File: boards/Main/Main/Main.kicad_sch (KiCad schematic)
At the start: 28 parts, among them J1 CAN_H, J10 Status_Light, J11 J00-0045NL, J12 IMU, J2 GND, J3 TX/RX, J4 5V, J5 Digital I/O, J6 CAN_Board, J7 CAN_L, J8 CAN H/L, J9 24V, K1 G5LE-1, K3 G5LE-1, K4 G5LE-1, Q1 2N3904, Q2 2N3904, Q3 2N3904, U1 Teensy4.1

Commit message: Updated Main PCB
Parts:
- removed J8: CAN H/L, Connector_PinHeader_2.54mm:PinHeader_1x01_P2.54mm_Vertical, symbol Connector_Generic:Conn_02x09_Row_Letter_First
- added CAN_OUT1: CAN_pins, Connector_PinHeader_2.54mm:PinHeader_2x09_P2.54mm_Vertical, symbol Connector_Generic:Conn_02x09_Top_Bottom
- added Ethernet_Cable1: Conn_02x03_Odd_Even, Connector_PinHeader_2.54mm:PinHeader_2x03_P2.54mm_Vertical, symbol Connector_Generic:Conn_02x03_Odd_Even
- 5V_Pin1: renamed from J4; footprint Connector_PinHeader_2.54mm:PinHeader_1x04_P2.54mm_Vertical -> Connector_PinHeader_2.54mm:PinHeader_1x02_P2.54mm_Vertical
- C1: renamed from 0.1uF1; value C -> 0.1uF
- D1, D2, D3: footprint LED_THT:LED_D5.0mm-3 -> LED_THT:LED_D5.0mm
- Relay_1: renamed from K1; value G5LE-1 -> G5LE1_Green
- Relay_2: renamed from K4; value G5LE-1 -> G5LE1_Blue
- Relay_3: renamed from K3; value G5LE-1 -> G5LE1_Red
- renumbered J9 to 24V_Pin1, J6 to CAN_Board1, J1 to CAN_H1, J7 to CAN_L1, J5 to Digital_I/O1, J11 to Ethernet1, J2 to GND_Pin1, J12 to IMU1, Q2 to Q1, Q1 to Q2, J3 to RTX_Pin1, J10 to Status_Light1, U1 to Teensy4.1
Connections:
- net M1H: now also CAN_OUT1.10 (Pin_10), CAN_OUT1.12 (Pin_12), CAN_OUT1.14 (Pin_14), CAN_OUT1.16 (Pin_16), CAN_OUT1.18 (Pin_18), CAN_OUT1.2 (Pin_2), CAN_OUT1.4 (Pin_4), CAN_OUT1.6 (Pin_6), CAN_OUT1.8 (Pin_8)
- net M1L: now also CAN_OUT1.1 (Pin_1), CAN_OUT1.11 (Pin_11), CAN_OUT1.13 (Pin_13), CAN_OUT1.15 (Pin_15), CAN_OUT1.17 (Pin_17), CAN_OUT1.3 (Pin_3), CAN_OUT1.5 (Pin_5), CAN_OUT1.7 (Pin_7), CAN_OUT1.9 (Pin_9)
- net at Teensy4.1.60 (R+): no longer Ethernet1.3 (RD+)
- net at Teensy4.1.61 (LED): no longer Ethernet1.9 (LA)
- net at Teensy4.1.62 (T-): no longer Ethernet1.2 (TD-)
- net at Teensy4.1.63 (T+): no longer Ethernet1.1 (TD+)
- net at C1.2, Ethernet1.10 (LC), Ethernet1.8 (GND): now also Ethernet_Cable1.3 (Pin_3); no longer Teensy4.1.64 (GND)
- net at Teensy4.1.65 (R-): no longer Ethernet1.6 (RD-)
- new net: Ethernet1.1 (TD+), Ethernet_Cable1.5 (Pin_5)
- new net: Ethernet1.2 (TD-), Ethernet_Cable1.6 (Pin_6)
- new net: Ethernet1.3 (RD+), Ethernet_Cable1.2 (Pin_2)
- new net: Ethernet1.6 (RD-), Ethernet_Cable1.1 (Pin_1)
- new net: Ethernet1.9 (LA), Ethernet_Cable1.4 (Pin_4)
- no-connect marks 50 -> 56
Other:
- moved on the sheet: RTX_Pin1, Status_Light1

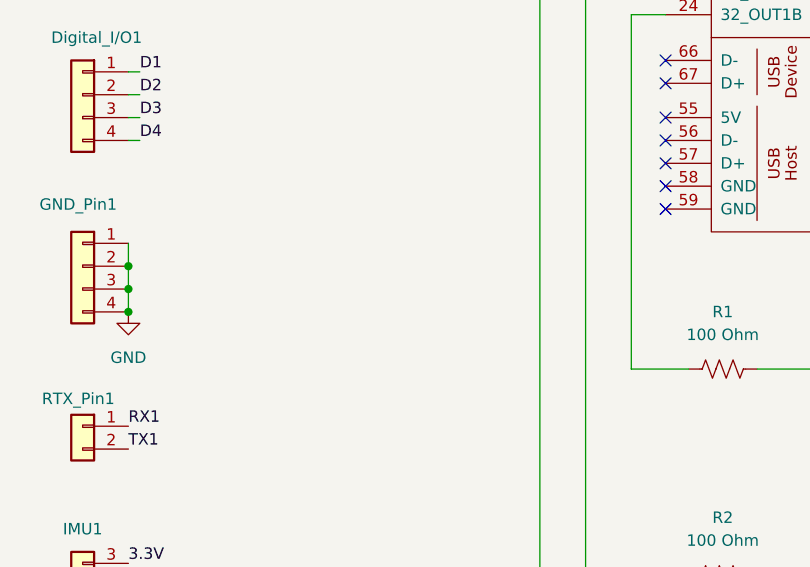
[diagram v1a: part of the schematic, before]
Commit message: Added Holes to Main PCB
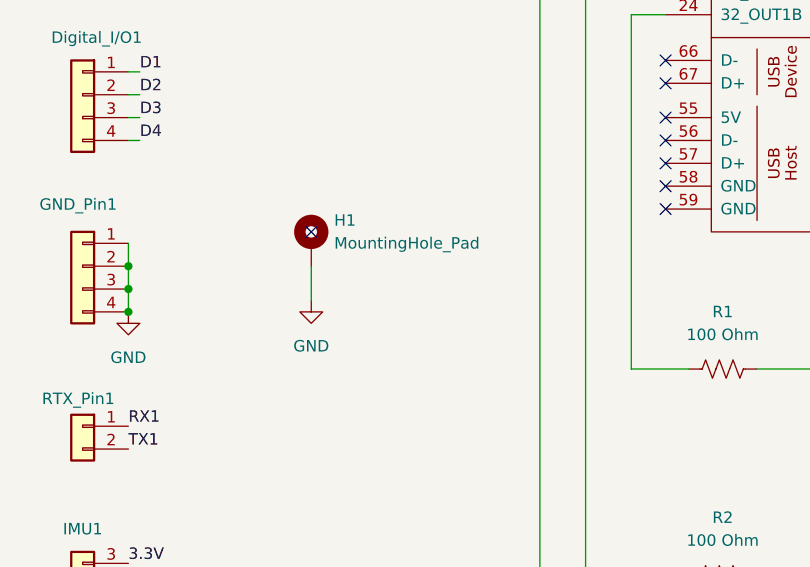
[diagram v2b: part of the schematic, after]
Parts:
- added H1: MountingHole_Pad, MountingHole:MountingHole_3.2mm_M3_DIN965_Pad_TopBottom, symbol Mechanical:MountingHole_Pad
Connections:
- net GND: now also H1.1
- no-connect marks 56 -> 57
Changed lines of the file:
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@@
+	)
+	(no_connect
+		(at 45.72 111.76)
 	)
 	(no_connect
@@
 		(pts
 			(xy 165.1 138.43) (xy 165.1 144.78)
+		)
+		(stroke
+			(width 0)
+			(type default)
+		)
+	)
+	(wire
+		(pts
+			(xy 45.72 115.57) (xy 45.72 119.38)
 		)
 		(stroke
@@
 				(path "/187ef870-6dee-45d7-ba09-9249896e2758"
 					(reference "R3")
+					(unit 1)
+				)
+			)
+		)
+	)
+	(symbol
+		(lib_id "power:GND")
+		(at 45.72 119.38 0)
+		(unit 1)
+		(exclude_from_sim no)
+		(in_bom yes)
+		(on_board yes)
+		(dnp no)
+		(fields_autoplaced yes)
+		(property "Reference" "#PWR017"
+			(at 45.72 125.73 0)
+			(effects
+				(font
+					(size 1.27 1.27)
+				)
+				(hide yes)
+			)
+		)
+		(property "Value" "GND"
+			(at 45.72 124.46 0)
+			(effects
+				(font
+					(size 1.27 1.27)
+				)
+			)
+		)
+		(property "Footprint" ""
+			(at 45.72 119.38 0)
+			(effects
+				(font
+					(size 1.27 1.27)
+				)
+				(hide yes)
+			)
+		)
+		(property "Datasheet" ""
+			(at 45.72 119.38 0)
+			(effects
+				(font
+					(size 1.27 1.27)
+				)
+				(hide yes)
+			)
+		)
+		(property "Description" "Power symbol creates a global label with name \"GND\" , ground"
+			(at 45.72 119.38 0)
+			(effects
+				(font
+					(size 1.27 1.27)
+				)
+				(hide yes)
+			)
+		)
+		(pin "1"
+		)
+		(instances
+			(project "Main"
+				(path "/187ef870-6dee-45d7-ba09-9249896e2758"
+					(reference "#PWR017")
 					(unit 1)
 				)
@@
 					(unit 1)
 				)
+			)
+		)
+	)
+	(symbol
+		(lib_id "Mechanical:MountingHole_Pad")
+		(at 45.72 113.03 0)
+		(unit 1)
+		(exclude_from_sim yes)
+		(in_bom no)
+		(on_board yes)
+		(dnp no)
+		(fields_autoplaced yes)
+		(property "Reference" "H1"
+			(at 48.26 110.4899 0)
+			(effects
+				(font
+					(size 1.27 1.27)
+				)
+				(justify left)
+			)
+		)
+		(property "Value" "MountingHole_Pad"
+			(at 48.26 113.0299 0)
+			(effects
+				(font
+					(size 1.27 1.27)
+				)
+				(justify left)
+			)
+		)
+		(property "Footprint" "MountingHole:MountingHole_3.2mm_M3_DIN965_Pad_TopBottom"
+			(at 45.72 113.03 0)
+			(effects
+				(font
+					(size 1.27 1.27)
+				)
+				(hide yes)
+			)
+		)
+		(property "Datasheet" "~"
+			(at 45.72 113.03 0)
+			(effects
+				(font
+					(size 1.27 1.27)
+				)
+				(hide yes)
+			)
+		)
+		(property "Description" "Mounting Hole with connection"
+			(at 45.72 113.03 0)
+			(effects
+				(font
+					(size 1.27 1.27)
+				)
+				(hide yes)
+			)
+		)
+		(pin "1"
+		)
+		(instances
+			(project "Main"
+				(path "/187ef870-6dee-45d7-ba09-9249896e2758"
+					(reference "H1")
+					(unit 1)
+				)

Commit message: updated main board
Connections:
- net 3.3V: now also CAN_Board1.2 (Pin_2), Teensy4.1.46 (3V3); no longer Teensy4.1.15 (3V3)
- no-connect marks 57 -> 58
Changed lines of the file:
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@@
+	)
+	(junction
+		(at 157.48 34.29)
+		(diameter 0)
+		(color 0 0 0 0)
 	)
 	(junction
@@
 	)
 	(no_connect
+		(at 85.09 64.77)
+	)
+	(no_connect
 		(at 85.09 52.07)
 	)
@@
 	(wire
 		(pts
-			(xy 140.97 34.29) (xy 160.02 34.29)
+			(xy 140.97 34.29) (xy 157.48 34.29)
 		)
 		(stroke
@@
 	(wire
 		(pts
+			(xy 157.48 26.67) (xy 157.48 34.29)
+		)
+		(stroke
+			(width 0)
+			(type default)
+		)
+	)
+	(wire
+		(pts
 			(xy 140.97 67.31) (xy 147.32 67.31)
 		)
@@
 	(wire
 		(pts
-			(xy 76.2 64.77) (xy 85.09 64.77)
-		)
-		(stroke
-			(width 0)
-			(type default)
-		)
-	)
-	(wire
-		(pts
 			(xy 163.83 96.52) (xy 163.83 85.09)
 		)
@@
 		(pts
 			(xy 158.75 170.18) (xy 165.1 170.18)
+		)
+		(stroke
+			(width 0)
+			(type default)
+		)
+	)
+	(wire
+		(pts
+			(xy 157.48 34.29) (xy 160.02 34.29)
 		)
 		(stroke
@@
 		)
 	)
-	(label "3.3V"
-		(at 76.2 64.77 0)
-		(fields_autoplaced yes)
-		(effects
-			(font
-				(size 1.27 1.27)
-			)
-			(justify left bottom)
-		)
-	)
 	(label "M3L"
 		(at 17.78 72.39 180)
@@
 		(fields_autoplaced yes)
 		(effects
+			(font
+				(size 1.27 1.27)
+			)
+			(justify left bottom)
+		)
+	)
+	(label "3.3V"
+		(at 157.48 26.67 0)
+		(fields_autoplaced yes)
+		(effects

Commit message: Add files via upload
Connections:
- net GND: no longer Teensy4.1.1 (GND)
- no-connect marks 58 -> 59
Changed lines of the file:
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@@
 	)
 	(junction
+		(at 147.32 31.75)
+		(diameter 0)
+		(color 0 0 0 0)
+	)
+	(junction
 		(at 190.5 48.26)
 		(diameter 0)
@@
 	)
 	(junction
-		(at 85.09 29.21)
-		(diameter 0)
-		(color 0 0 0 0)
-	)
-	(junction
 		(at 130.81 119.38)
 		(diameter 0)
@@
 	)
 	(no_connect
+		(at 85.09 29.21)
+	)
+	(no_connect
 		(at 85.09 109.22)
 	)
@@
 	(wire
 		(pts
+			(xy 147.32 31.75) (xy 151.13 31.75)
+		)
+		(stroke
+			(width 0)
+			(type default)
+		)
+	)
+	(wire
+		(pts
 			(xy 144.78 160.02) (xy 144.78 167.64)
 		)
@@
 	(wire
 		(pts
-			(xy 140.97 31.75) (xy 151.13 31.75)
+			(xy 140.97 31.75) (xy 147.32 31.75)
 		)
 		(stroke
@@
 	(wire
 		(pts
-			(xy 77.47 29.21) (xy 85.09 29.21)
-		)
-		(stroke
-			(width 0)
-			(type default)
-		)
-	)
-	(wire
-		(pts
 			(xy 130.81 170.18) (xy 146.05 170.18)
 		)
@@
 	)
 	(symbol
-		(lib_id "power:PWR_FLAG")
-		(at 85.09 29.21 0)
-		(unit 1)
-		(exclude_from_sim no)
-		(in_bom yes)
-		(on_board yes)
-		(dnp no)
-		(fields_autoplaced yes)
-		(property "Reference" "#FLG03"
-			(at 85.09 27.305 0)
-			(effects
-				(font
-					(size 1.27 1.27)
-				)
-				(hide yes)
-			)
-		)
-		(property "Value" "PWR_FLAG"
-			(at 85.09 24.13 0)
-			(effects
-				(font
-					(size 1.27 1.27)
-				)
-				(hide yes)
-			)
-		)
-		(property "Footprint" ""
-			(at 85.09 29.21 0)
-			(effects
-				(font
-					(size 1.27 1.27)
-				)
-				(hide yes)
-			)
-		)
-		(property "Datasheet" "~"
-			(at 85.09 29.21 0)
-			(effects
-				(font
-					(size 1.27 1.27)
-				)
-				(hide yes)
-			)
-		)
-		(property "Description" "Special symbol for telling ERC where power comes from"
-			(at 85.09 29.21 0)
-			(effects
-				(font
-					(size 1.27 1.27)
-				)
-				(hide yes)
-			)
-		)
-		(pin "1"
-		)
-		(instances
-			(project "Main"
-				(path "/187ef870-6dee-45d7-ba09-9249896e2758"
-					(reference "#FLG03")
-					(unit 1)
-				)
-			)
-		)
-	)
-	(symbol
-		(lib_id "power:GND")
-		(at 77.47 29.21 180)
-		(unit 1)
-		(exclude_from_sim no)
-		(in_bom yes)
-		(on_board yes)
-		(dnp no)
-		(fields_autoplaced yes)
-		(property "Reference" "#PWR010"
-			(at 77.47 22.86 0)
-			(effects
-				(font
-					(size 1.27 1.27)
-				)
-				(hide yes)
-			)
-		)
-		(property "Value" "GND"
-			(at 77.47 24.13 0)
-			(effects
-				(font
-					(size 1.27 1.27)
-				)
-			)
-		)
-		(property "Footprint" ""
-			(at 77.47 29.21 0)
-			(effects
-				(font
-					(size 1.27 1.27)
-				)
-				(hide yes)
-			)
-		)
-		(property "Datasheet" ""
-			(at 77.47 29.21 0)
-			(effects
-				(font
-					(size 1.27 1.27)
-				)
-				(hide yes)
-			)
-		)
-		(property "Description" "Power symbol creates a global label with name \"GND\" , ground"
-			(at 77.47 29.21 0)
-			(effects
-				(font
-					(size 1.27 1.27)
-				)
-				(hide yes)
-			)
-		)
-		(pin "1"
-		)
-		(instances
-			(project "Main"
-				(path "/187ef870-6dee-45d7-ba09-9249896e2758"
-					(reference "#PWR010")
-					(unit 1)
-				)
-			)
-		)
-	)
-	(symbol
 		(lib_id "Transistor_BJT:2N3904")
 		(at 106.68 149.86 0)
@@
 					(unit 1)
 				)
+			)
+		)
+	)
+	(symbol
+		(lib_id "power:PWR_FLAG")
+		(at 147.32 31.75 0)
+		(unit 1)
+		(exclude_from_sim no)
+		(in_bom yes)
+		(on_board yes)
+		(dnp no)
+		(fields_autoplaced yes)
+		(property "Reference" "#FLG03"
+			(at 147.32 29.845 0)
+			(effects
+				(font
+					(size 1.27 1.27)
+				)
+				(hide yes)
+			)
+		)
+		(property "Value" "PWR_FLAG"
+			(at 147.32 26.67 0)
+			(effects
+				(font
+					(size 1.27 1.27)
+				)
+				(hide yes)
+			)
+		)
+		(property "Footprint" ""
+			(at 147.32 31.75 0)
+			(effects
+				(font
+					(size 1.27 1.27)
+				)
+				(hide yes)
+			)
+		)
+		(property "Datasheet" "~"
+			(at 147.32 31.75 0)
+			(effects
+				(font
+					(size 1.27 1.27)
+				)
+				(hide yes)
+			)
+		)
+		(property "Description" "Special symbol for telling ERC where power comes from"
+			(at 147.32 31.75 0)
+			(effects
+				(font
+					(size 1.27 1.27)
+				)
+				(hide yes)
+			)
+		)
+		(pin "1"
+		)
+		(instances
+			(project "Main"
+				(path "/187ef870-6dee-45d7-ba09-9249896e2758"
+					(reference "#FLG03")
+					(unit 1)
+				)

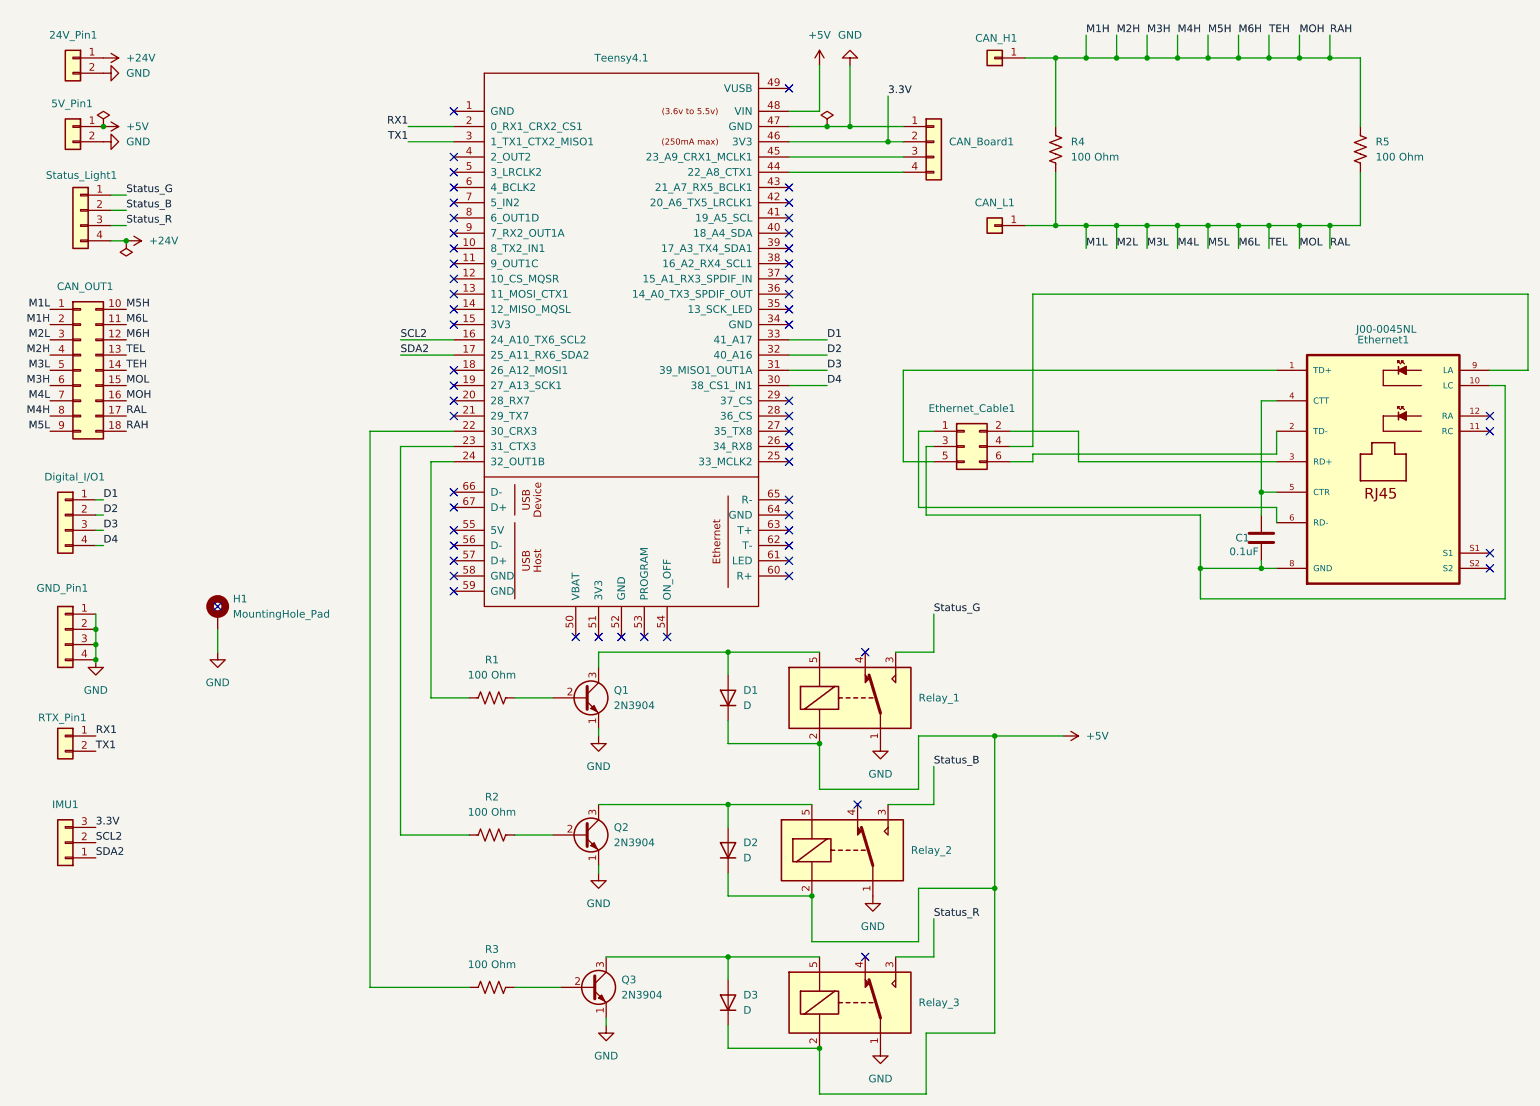
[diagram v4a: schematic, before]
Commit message: Prepared Boards for PCB Manufacture
Added GND line for IMU on Main Board
Fixed Silkscreen Text Size for PCB Manufacture on Science, Main, and Arm boards
Generated Gerber Files for Science, Main, and Arm boards
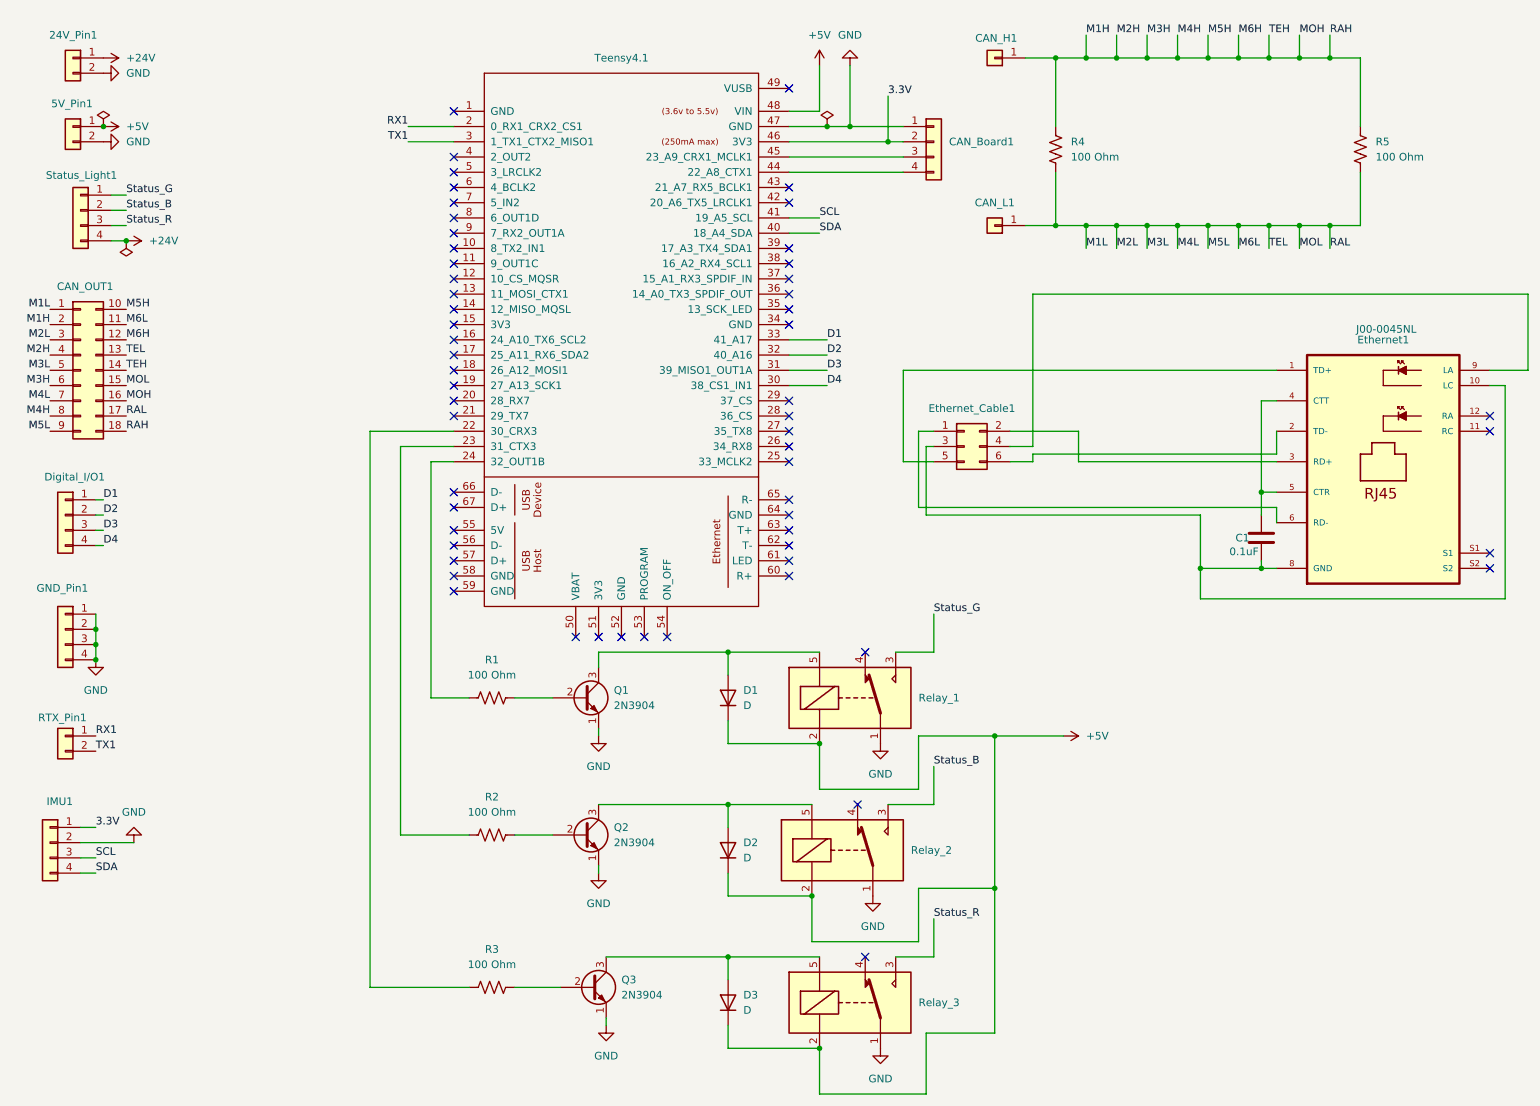
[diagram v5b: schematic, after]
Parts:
- removed H1: MountingHole_Pad, MountingHole:MountingHole_3.2mm_M3_DIN965_Pad_TopBottom, symbol Mechanical:MountingHole_Pad
- removed IMU1: IMU, Connector_PinHeader_2.54mm:PinHeader_1x03_P2.54mm_Vertical, symbol Connector_Generic:Conn_01x03
- added IMU1: GND, Connector_PinHeader_2.54mm:PinHeader_1x04_P2.54mm_Vertical, symbol Connector_Generic:Conn_01x04
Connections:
- net 3.3V: now also IMU1.1 (Pin_1)
- net GND: now also IMU1.2 (Pin_2)
- net SDA: now reaches Teensy4.1.40 (18_A4_SDA)
- net SDA: now also IMU1.4 (Pin_4)
- net SCL: now reaches Teensy4.1.41 (19_A5_SCL)
- net SCL: now also IMU1.3 (Pin_3)
- net SCL2: no longer names the net of Teensy4.1.16 (24_A10_TX6_SCL2)
- net SDA2: no longer names the net of Teensy4.1.17 (25_A11_RX6_SDA2)
- no-connect marks 59 -> 58
